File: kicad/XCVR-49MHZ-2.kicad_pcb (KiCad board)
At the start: 4 copper layers, 55 x 35 mm, 63 parts, among them U1 ByA 100nF +3V3 U1-VDDA Bypass, U1 ByB 100nF +3V3 U1-VDD Bypass

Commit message: updated px
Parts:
- UART CMC: footprint L_0402_1005Metric -> SRF2012_2012Metric
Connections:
- AFSK Cp pad 2: AFSK_OUT -> AFSK_IN
- PA Cb1 pad 2: DDS_RF -> PA_INT
- PA Re pad 1: GND -> PA_EMIT
- RX Bead pad 1: UART_RX -> UART_RX_F
- RX Bead pad 2: UART_RX -> UART_RX_F
- TX Bead pad 1: UART_TX -> UART_TX_F
- TX Bead pad 2: UART_TX -> UART_TX_F
- Th Lo pad 1: GND -> COMP_IN
- UART CMC pad 2: UART_TX -> UART_TX_F
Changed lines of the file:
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@@
 	(net 25 "RF_ANT_SW")
 	(net 26 "COMP_IN")
+	(net 27 "UART_TX_F")
+	(net 28 "UART_RX_F")
+	(net 29 "PA_EMIT")
+	(net 30 "SBUS_OUT")
+	(net 31 "MODE_SEL")
+	(net 32 "UART_RX_MUX")
 	(footprint "C_0402_1005Metric"
 		(layer "F.Cu")
@@
 			(layers "F.Cu" "F.Mask" "F.Paste")
 			(roundrect_rratio 0.25)
-			(net 1 "GND")
+			(net 29 "PA_EMIT")
 		)
 		(pad "2" smd roundrect
@@
 			(layers "F.Cu" "F.Mask" "F.Paste")
 			(roundrect_rratio 0.25)
-			(net 4 "UART_TX")
+			(net 27 "UART_TX_F")
 		)
 		(pad "2" smd roundrect
@@
 			(layers "F.Cu" "F.Mask" "F.Paste")
 			(roundrect_rratio 0.25)
-			(net 4 "UART_TX")
+			(net 27 "UART_TX_F")
 		)
 		(embedded_fonts no)
@@
 		)
 	)
-	(footprint "L_0402_1005Metric"
+	(footprint "SRF2012_2012Metric"
 		(layer "F.Cu")
 		(at 106.485 110.5)
-		(descr "Inductor SMD 0402 (1005 Metric), square (rectangular) end terminal, IPC-7351 nominal, (Body size source: http://www.tortai-tech.com/upload/download/2011102023233369053.pdf), generated with kicad-footprint-generator")
-		(tags "inductor")
+		(descr "Bourns SRF2012-100Y Common-Mode Choke, SMD 2.0x1.25mm 4-pad; winding-1 pins 1+2 carry UART_TX, winding-2 pins 4+3 carry UART_RX")
+		(tags "inductor common-mode choke CMC SRF2012 UART")
 		(property "Reference" "UART CMC"
-			(at 0 -1.17 0)
+			(at 0 -1.7 0)
 			(layer "F.SilkS")
 			(effects
@@
 		)
 		(property "Value" "SRF2012-100Y  CMC  UART TX/RX Pair 10uH"
-			(at -41.5 1.5 90)
+			(at 0 1.9 0)
 			(layer "F.Fab")
 			(effects
 				(font
-					(size 0.8 0.8)
-					(thickness 0.12)
+					(size 0.5 0.5)
+					(thickness 0.08)
 				)
 			)
@@
 		(attr smd)
 		(fp_line
-			(start -0.93 -0.47)
-			(end 0.93 -0.47)
+			(start -0.85 -0.72)
+			(end 0.85 -0.72)
+			(stroke
+				(width 0.12)
+				(type solid)
+			)
+			(layer "F.SilkS")
+		)
+		(fp_line
+			(start -0.85 0.72)
+			(end 0.85 0.72)
+			(stroke
+				(width 0.12)
+				(type solid)
+			)
+			(layer "F.SilkS")
+		)
+		(fp_poly
+			(pts
+				(xy -1.1 -0.92) (xy -1.35 -1.22) (xy -0.85 -1.22) (xy -1.1 -0.92)
+			)
+			(stroke
+				(width 0.12)
+				(type solid)
+			)
+			(fill yes)
+			(layer "F.SilkS")
+		)
+		(fp_line
+			(start -1.2 -0.92)
+			(end 1.2 -0.92)
 			(stroke
 				(width 0.05)
@@
 		)
 		(fp_line
-			(start -0.93 0.47)
-			(end -0.93 -0.47)
+			(start -1.2 0.92)
+			(end -1.2 -0.92)
 			(stroke
 				(width 0.05)
@@
 		)
 		(fp_line
-			(start 0.93 -0.47)
-			(end 0.93 0.47)
+			(start 1.2 -0.92)
+			(end 1.2 0.92)
 			(stroke
 				(width 0.05)
@@
 		)
 		(fp_line
-			(start 0.93 0.47)
-			(end -0.93 0.47)
+			(start 1.2 0.92)
+			(end -1.2 0.92)
 			(stroke
 				(width 0.05)
@@
 		)
 		(fp_line
-			(start -0.5 -0.25)
-			(end 0.5 -0.25)
+			(start -1.0 -0.625)
+			(end 1.0 -0.625)
 			(stroke
 				(width 0.1)
@@
 		)
 		(fp_line
-			(start -0.5 0.25)
-			(end -0.5 -0.25)
+			(start -1.0 0.625)
+			(end -1.0 -0.625)
 			(stroke
 				(width 0.1)
@@
 		)
 		(fp_line
-			(start 0.5 -0.25)
-			(end 0.5 0.25)
+			(start 1.0 -0.625)
+			(end 1.0 0.625)
 			(stroke
 				(width 0.1)
@@
 		)
 		(fp_line
-			(start 0.5 0.25)
-			(end -0.5 0.25)
+			(start 1.0 0.625)
+			(end -1.0 0.625)
 			(stroke
 				(width 0.1)
@@
 			(effects
 				(font
-					(size 0.25 0.25)
-					(thickness 0.04)
+					(size 0.4 0.4)
+					(thickness 0.06)
 				)
 			)
 		)
 		(pad "1" smd roundrect
-			(at -0.485 0)
-			(size 0.59 0.64)
+			(at -0.65 -0.375)
+			(size 0.55 0.55)
 			(layers "F.Cu" "F.Mask" "F.Paste")
 			(roundrect_rratio 0.25)
@@
 		)
 		(pad "2" smd roundrect
-			(at 0.485 0)
-			(size 0.59 0.64)
+			(at 0.65 -0.375)
+			(size 0.55 0.55)
 			(layers "F.Cu" "F.Mask" "F.Paste")
 			(roundrect_rratio 0.25)
-			(net 4 "UART_TX")
+			(net 27 "UART_TX_F")
+		)
+		(pad "3" smd roundrect
+			(at 0.65 0.375)
+			(size 0.55 0.55)
+			(layers "F.Cu" "F.Mask" "F.Paste")
+			(roundrect_rratio 0.25)
+			(net 28 "UART_RX_F")
+		)
+		(pad "4" smd roundrect
+			(at -0.65 0.375)
+			(size 0.55 0.55)
+			(layers "F.Cu" "F.Mask" "F.Paste")
+			(roundrect_rratio 0.25)
+			(net 5 "UART_RX")
 		)
 		(embedded_fonts no)
-		(model "${KICAD9_3DMODEL_DIR}/Inductor_SMD.3dshapes/L_0402_1005Metric.step"
+		(model "${KICAD9_3DMODEL_DIR}/Filter.3dshapes/Bourns_SRF2012.step"
 			(offset
 				(xyz 0 0 0)
@@
 		(tags "resistor")
 		(property "Reference" "RSSI Lo"
-			(at 2 3.5 0)
+			(at 0 -1.17 0)
 			(layer "F.SilkS")
 			(effects
@@
 		(tags "resistor")
 		(property "Reference" "Th Lo"
-			(at 0 6.5 0)
+			(at 0 -1.17 0)
 			(layer "F.SilkS")
 			(effects
@@
 			(layers "F.Cu" "F.Mask" "F.Paste")
 			(roundrect_rratio 0.25)
-			(net 1 "GND")
+			(net 26 "COMP_IN")
 		)
 		(pad "2" smd roundrect
@@
 			(layers "F.Cu" "F.Mask" "F.Paste")
 			(roundrect_rratio 0.25)
-			(net 5 "UART_RX")
+			(net 28 "UART_RX_F")
 		)
 		(pad "2" smd roundrect
@@
 			(layers "F.Cu" "F.Mask" "F.Paste")
 			(roundrect_rratio 0.25)
-			(net 5 "UART_RX")
+			(net 28 "UART_RX_F")
 		)
 		(embedded_fonts no)
@@
 			(layers "F.Cu" "F.Mask" "F.Paste")
 			(roundrect_rratio 0.25)
-			(net 17 "DDS_RF")
+			(net 18 "PA_INT")
 		)
 		(embedded_fonts no)
@@
 			(layers "F.Cu" "F.Mask" "F.Paste")
 			(roundrect_rratio 0.25)
-			(net 14 "AFSK_OUT")
+			(net 15 "AFSK_IN")
 		)
 		(embedded_fonts no)

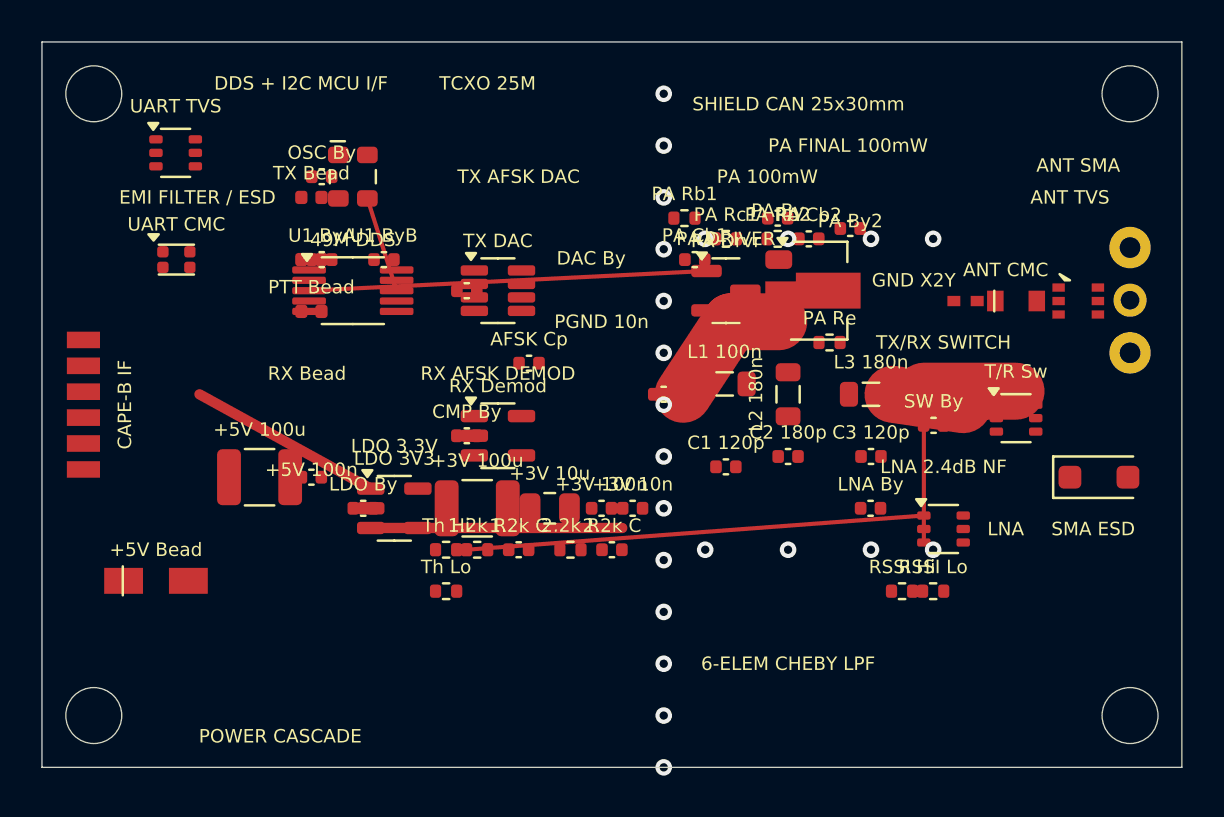
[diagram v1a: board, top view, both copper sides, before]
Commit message: updated the xcvr to fix drc issues an
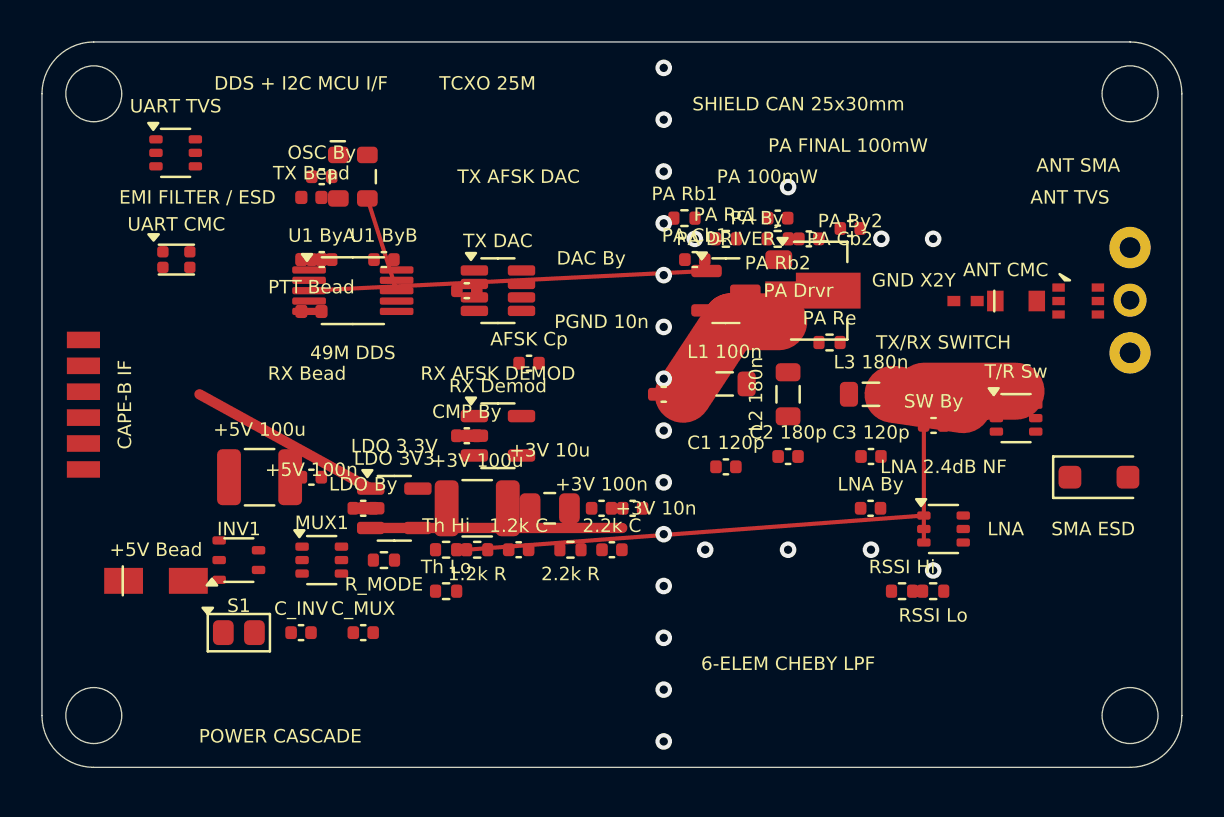
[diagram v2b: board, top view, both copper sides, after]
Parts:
- added C_INV: 100nF C0G 0402 INV1 VCC Bypass, C_0402_1005Metric, F.Cu at (112.5, 128.5)
- added C_MUX: 100nF C0G 0402 MUX1 VCC Bypass, C_0402_1005Metric, F.Cu at (115.5, 128.5)
- added INV1: SN74LVC1G04 SOT-23-5 3.3V UART_RX_F->SBUS_OUT, SOT-23-5, F.Cu at (109.5, 125.0)
- added MUX1: SN74LVC1G157 SC-70-6 2:1MUX UART/SBUS Select, SOT-363_SC-70-6, F.Cu at (113.5, 125.0)
- added R_MODE: 10k Ohm MODE_SEL Pull-Down UART=default, R_0402_1005Metric, F.Cu at (116.5, 125.0)
- added S1: SPST-SMD OPEN=UART CLOSED=SBUS, SW_SPST_SMD_2Pin, F.Cu at (109.5, 128.5)
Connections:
- UART CMC pad 3: UART_RX_F -> UART_RX_MUX
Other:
- outline, holes or cut-outs redrawn
